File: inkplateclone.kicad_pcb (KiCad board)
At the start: 2 copper layers, 88 parts, among them J1 ED060SC7, J2 USB_C_Receptacle_USB2.0, J3 Conn_01x03_Male, Q1 Q_NMOS_GSD, Q2 Q_NMOS_GSD, Q3 Q_PMOS_GSD, U1 TPS65186, U2 ED097OC1, U3 MCP23017_SO, U4 ESP32-WROVER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

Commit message: routed switches and added 3d models
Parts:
- added J4: Conn_01x03_Male, Connector_PinHeader_2.54mm:PinHeader_1x03_P2.54mm_Vertical, F.Cu at (106.1, 125.4)
- added SW1: SW_Push, Button_Switch_SMD:SW_Push_1P1T_NO_6x6mm_H9.5mm, F.Cu at (125.6, 120.4)
- added SW2: SW_Push, Button_Switch_SMD:SW_Push_1P1T_NO_6x6mm_H9.5mm, F.Cu at (125.5, 112.0)
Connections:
- net /I2C_SCL renamed I2C_SCL
- net /I2C_SDA renamed I2C_SDA
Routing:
- net ESP_RXD: track 0.00 -> 15.5 mm
- net ESP_TXD: track 0.00 -> 12.5 mm
- net RST: track 4.19 -> 9.92 mm
- net EPD_CL: track 4.05 -> 9.63 mm
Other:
- board text added: "Flash"
- board text added: "GND"
- board text added: "RX"
- board text added: "Reset"
- board text added: "TX"

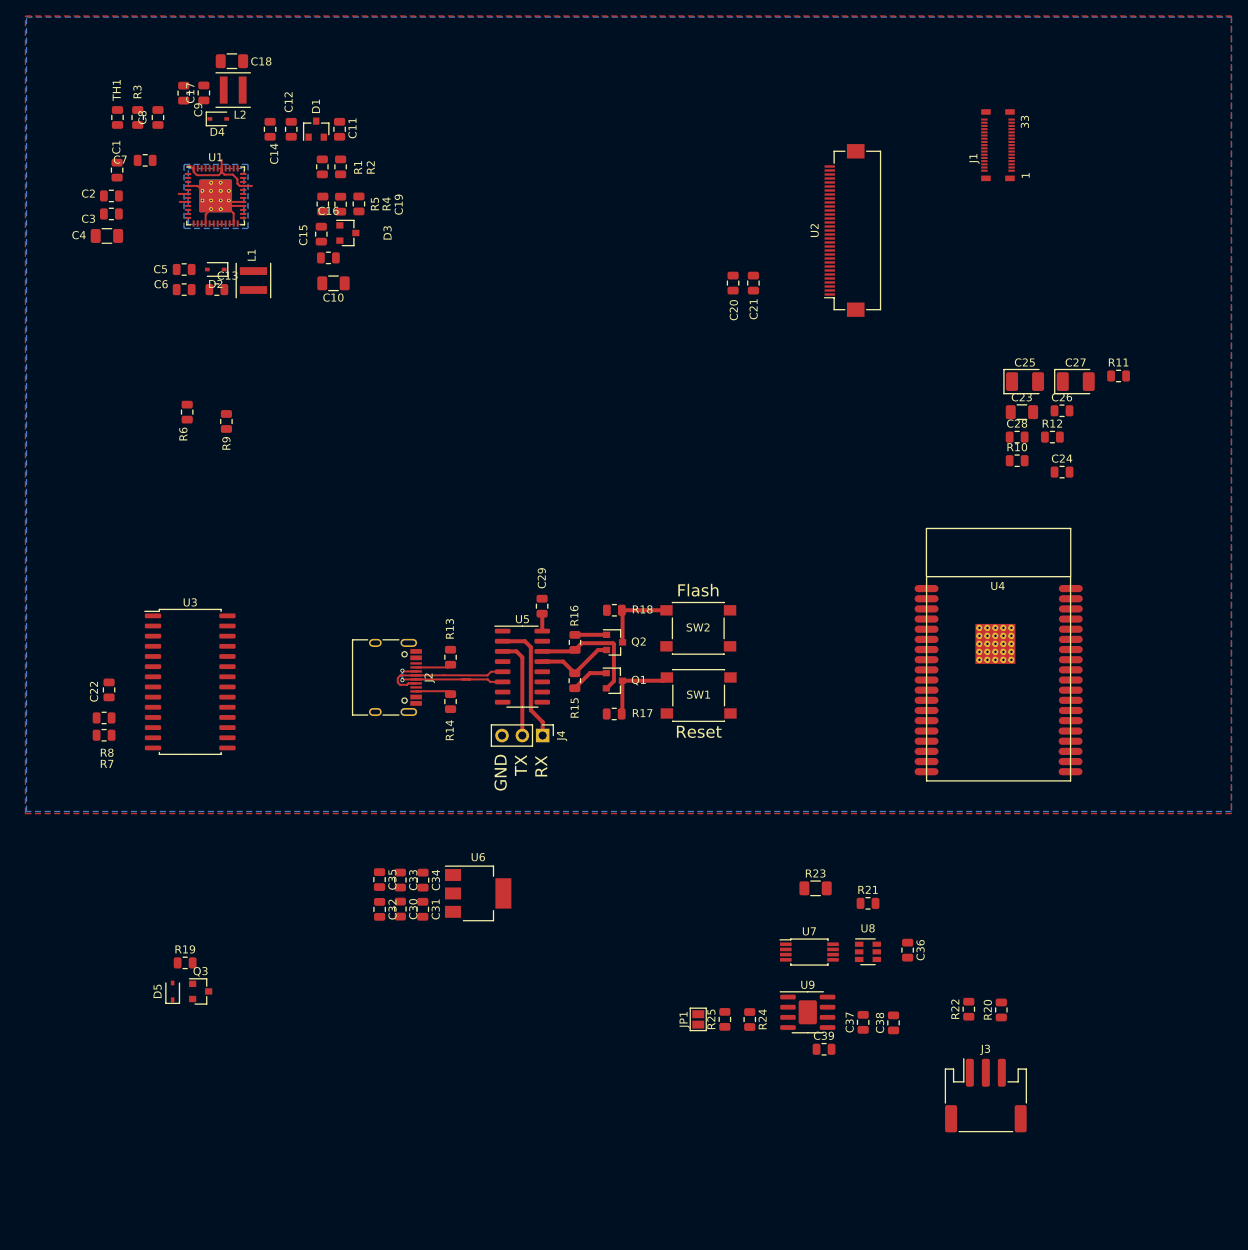
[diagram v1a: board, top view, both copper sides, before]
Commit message: routed charger and ideal diode
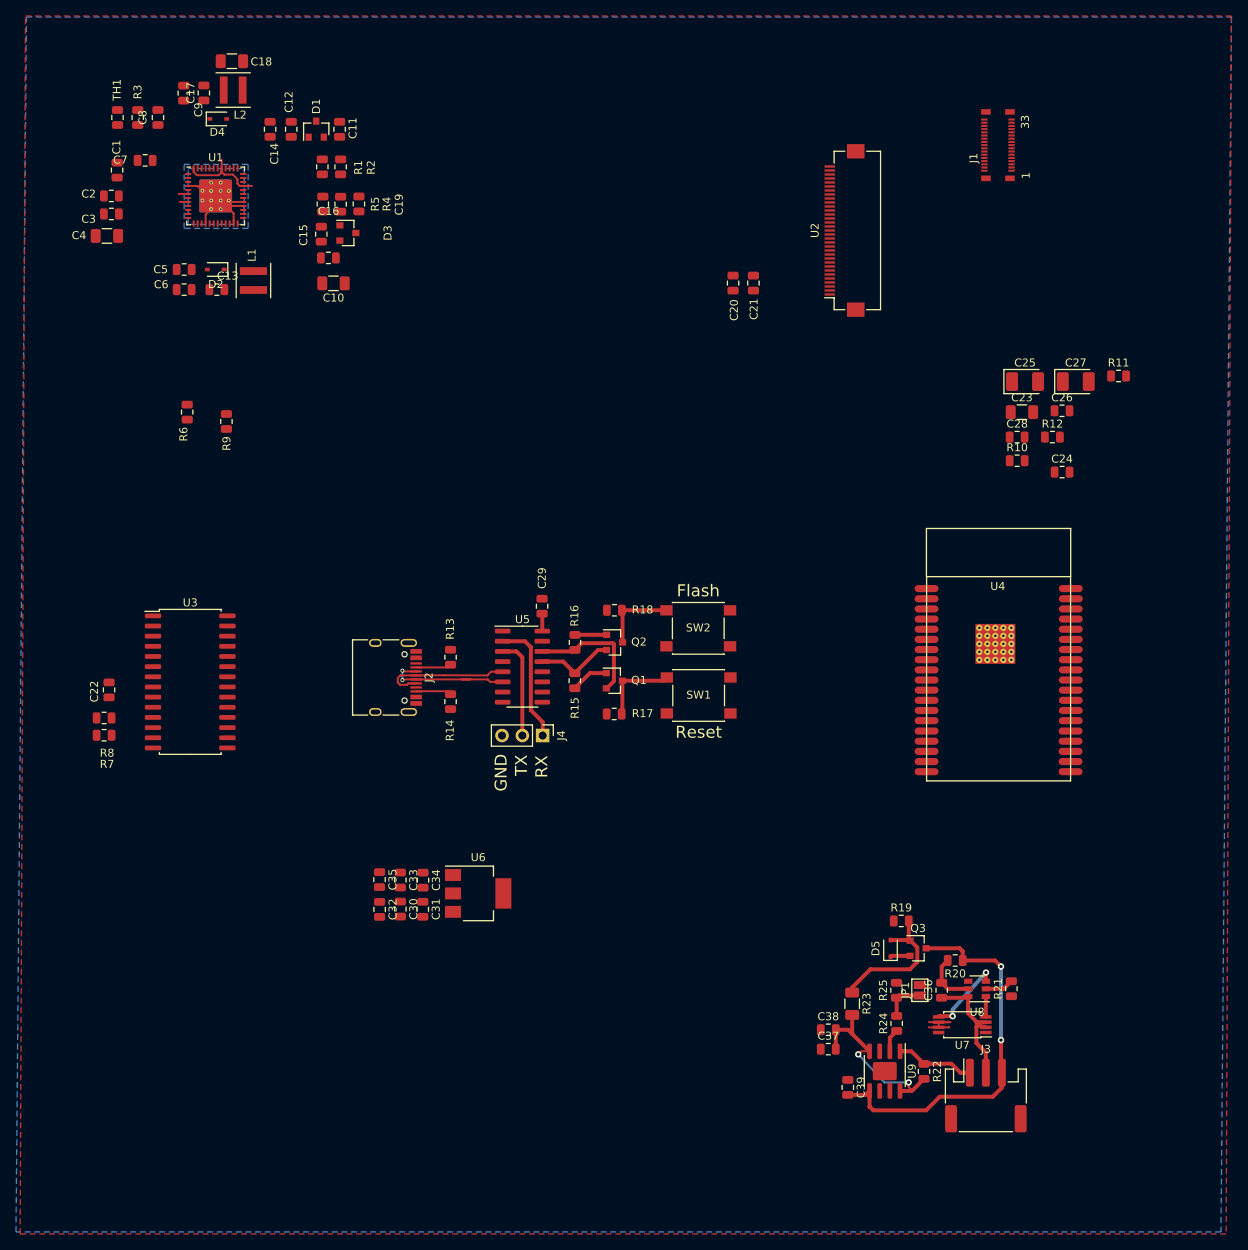
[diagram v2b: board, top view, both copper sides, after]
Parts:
- moved D5 89.9 mm to (149.5, 152.0)
- moved Q3 89.8 mm to (153.0, 152.0)
- moved R19 89.7 mm to (150.9, 148.6)
- moved JP1 27.9 mm to (153.2, 157.2)
- moved R25 21.8 mm to (150.3, 157.2)
- moved U7 21.2 mm to (158.5, 161.5), turned to 180 degrees
- moved R21 20.9 mm to (164.6, 157.0), turned to 90 degrees
- moved R24 18.4 mm to (150.3, 161.4), turned to 90 degrees
- moved R23 15.1 mm to (144.7, 158.9), turned to 270 degrees
- moved U8 14.4 mm to (160.4, 157.0), turned to 180 degrees
- moved U9 12.1 mm to (148.8, 167.3), turned to 270 degrees
- moved R22 9.58 mm to (153.7, 167.4), turned to 270 degrees
- moved R20 8.45 mm to (157.6, 153.5), turned to 180 degrees
- moved C38 8.20 mm to (141.8, 162.2), turned to 0 degrees
- moved C36 6.58 mm to (155.9, 157.2), turned to 90 degrees
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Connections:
- net /SPI_NCS renamed SPI_NCS
- net /SPI_SCL renamed SPI_SCL
- net /SPI_SDI renamed SPI_SDI
- J3 pad 3: /BAT_POS -> VBAT
- R20 pad 1: /BAT_POS -> VBAT
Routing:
- net VBAT: track 0.00 -> 49.0 mm, vias 0 -> 2
- net Net-(C37-Pad2): track 0.00 -> 24.4 mm, vias 0 -> 2
- net +5V: track 2.18 -> 20.3 mm
- net /BAT_GND: track 0.00 -> 16.4 mm
- net Net-(U7-Pad5): track 0.00 -> 9.92 mm, vias 0 -> 2
- net BAT_TMP: track 0.00 -> 9.86 mm
- net Net-(C36-Pad2): track 0.00 -> 6.74 mm
- net Net-(JP1-Pad1): track 0.00 -> 5.33 mm
- net GND: track 14.2 -> 19.4 mm
- net Net-(R21-Pad2): track 0.00 -> 3.58 mm
- net Net-(R24-Pad1): track 0.00 -> 2.89 mm
- net Net-(U7-Pad4): track 0.00 -> 2.54 mm
- net VIN: track 0.00 -> 2.50 mm

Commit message: routed voltage regulator
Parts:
- added J5: Conn_01x02_Male, Connector_PinHeader_2.54mm:PinHeader_1x02_P2.54mm_Vertical, F.Cu at (93.3, 125.4)
- moved C32 52.9 mm to (135.6, 164.7), turned to 0 degrees
- moved C35 50.9 mm to (131.9, 164.7), turned to 0 degrees
- moved C30 49.6 mm to (135.6, 162.1), turned to 0 degrees
- moved C33 47.5 mm to (131.9, 162.1), turned to 0 degrees
- moved C31 46.2 mm to (135.6, 159.3), turned to 0 degrees
- moved C34 43.8 mm to (132.0, 159.3), turned to 0 degrees
- moved U6 36.4 mm to (133.6, 152.4), turned to 90 degrees
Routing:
- net VIN: track 2.50 -> 27.5 mm
- net +3V3: track 0.00 -> 15.9 mm
- net RST: track 9.92 -> 17.9 mm
- net EPD_CL: track 9.63 -> 17.6 mm
- net +5V: track 20.3 -> 27.6 mm
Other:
- board text added: "+5v"

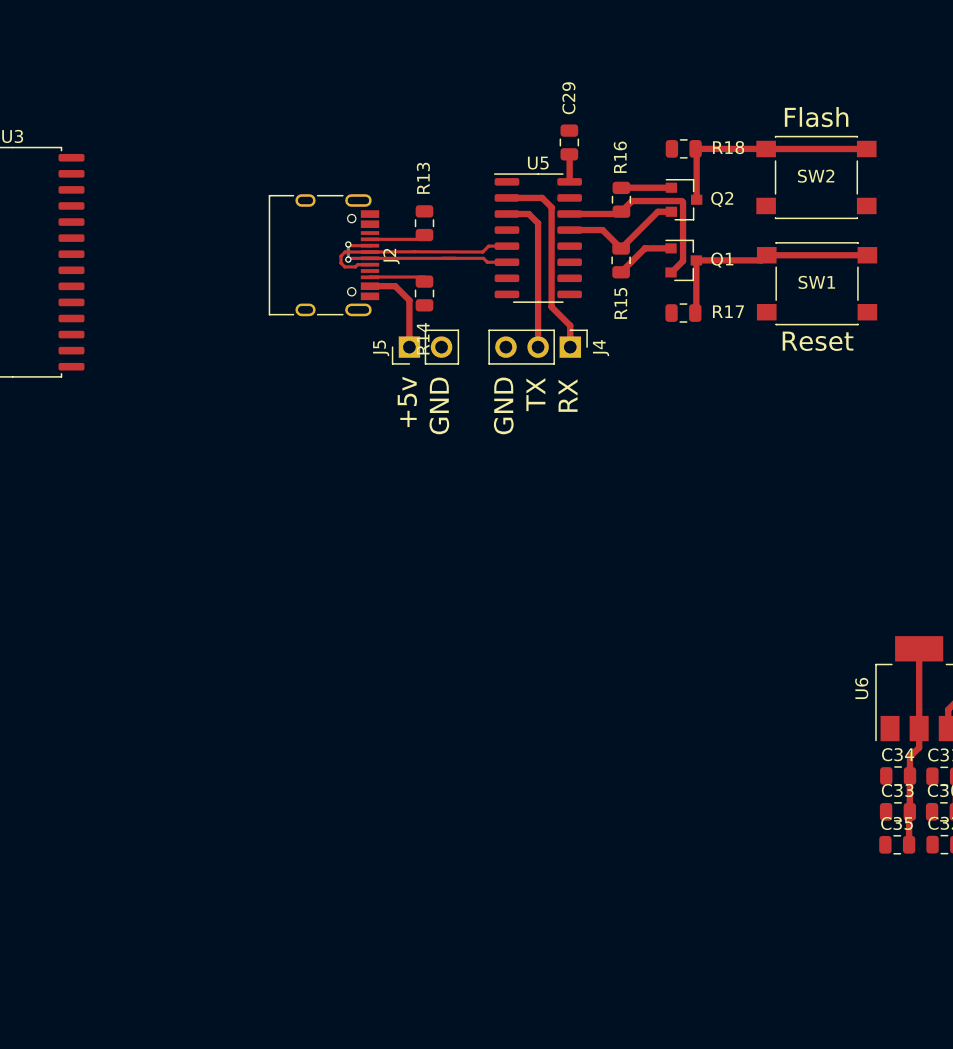
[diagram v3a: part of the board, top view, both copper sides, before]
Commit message: added 3d model for battery connector
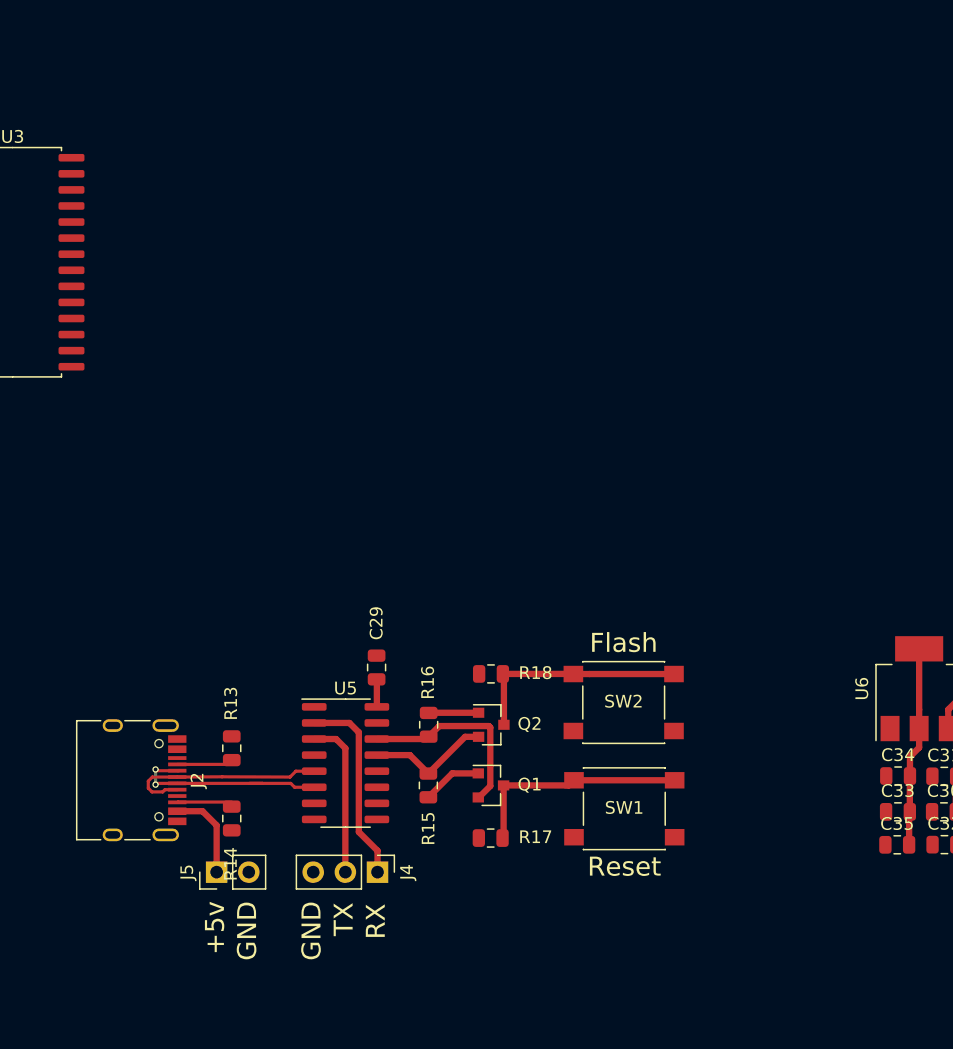
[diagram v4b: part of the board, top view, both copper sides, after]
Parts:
- moved J2 44.2 mm to (71.0, 159.6)
- moved Q1 44.2 mm to (99.8, 160.0)
- moved R15 44.2 mm to (94.8, 160.0)
- moved R18 44.2 mm to (99.8, 151.2)
- moved J4 44.2 mm to (90.8, 166.9)
- moved J5 44.2 mm to (78.1, 166.9)
- moved R13 44.2 mm to (79.3, 157.1)
- moved R17 44.2 mm to (99.8, 164.2)
- moved SW1 44.2 mm to (110.3, 161.8)
- moved SW2 44.2 mm to (110.3, 153.5)
- moved C29 44.2 mm to (90.8, 150.7)
- moved Q2 44.2 mm to (99.8, 155.2)
- moved R14 44.2 mm to (79.3, 162.6)
- moved R16 44.2 mm to (94.9, 155.2)
- moved U5 44.2 mm to (88.3, 158.2)

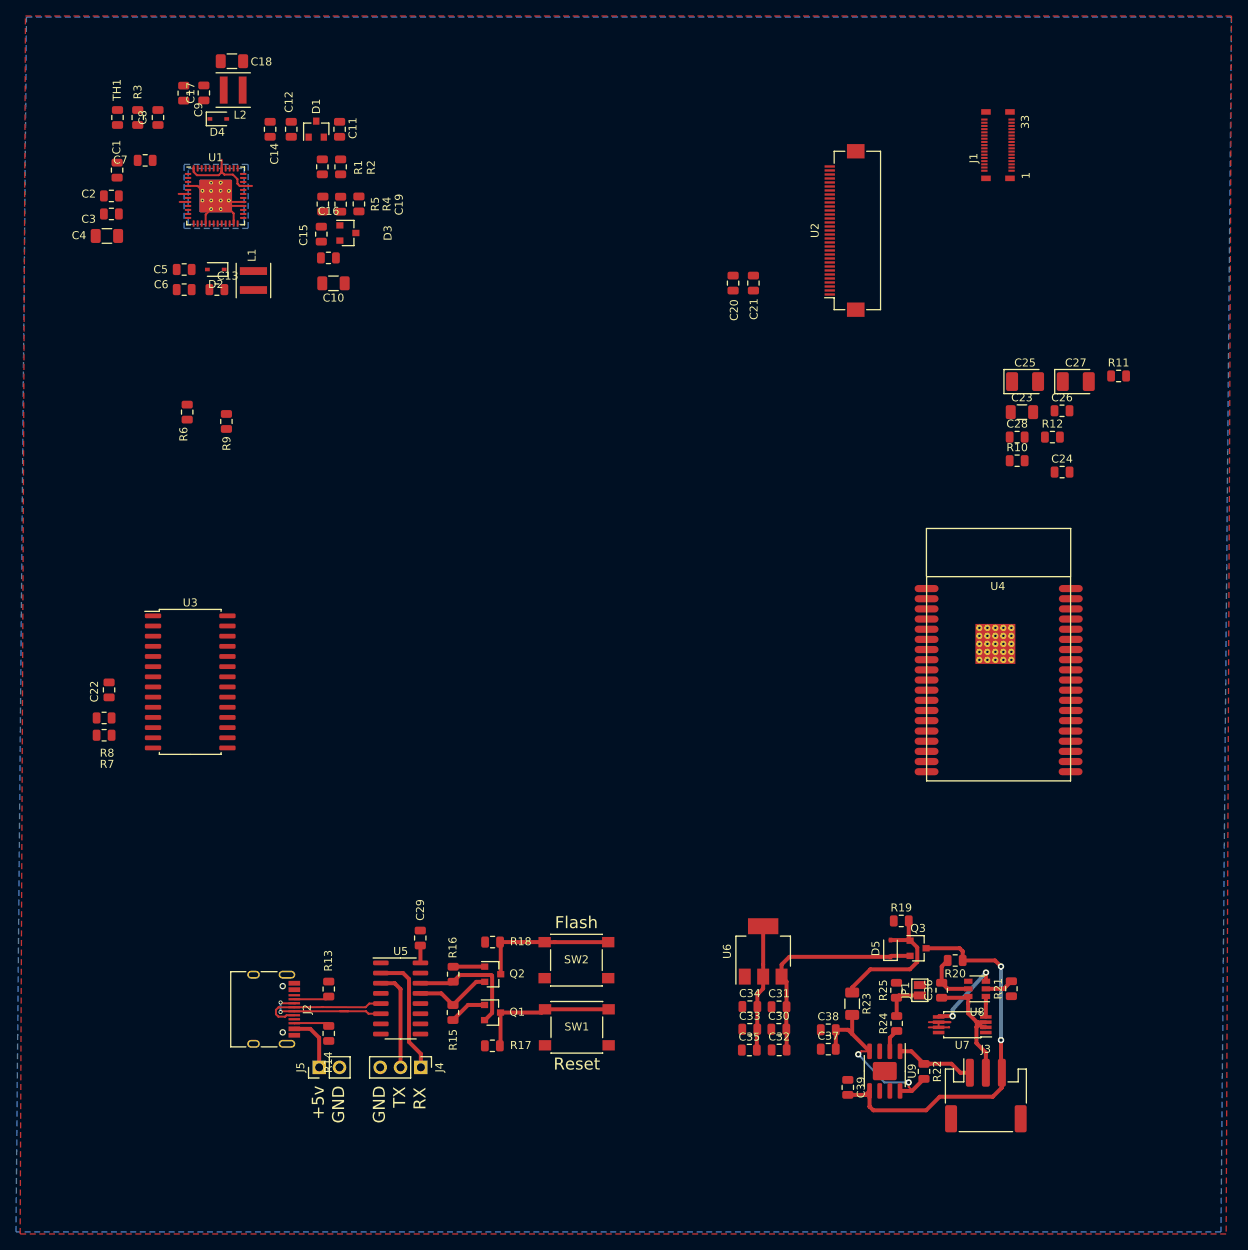
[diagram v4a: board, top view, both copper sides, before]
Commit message: cleaned up silkscreen
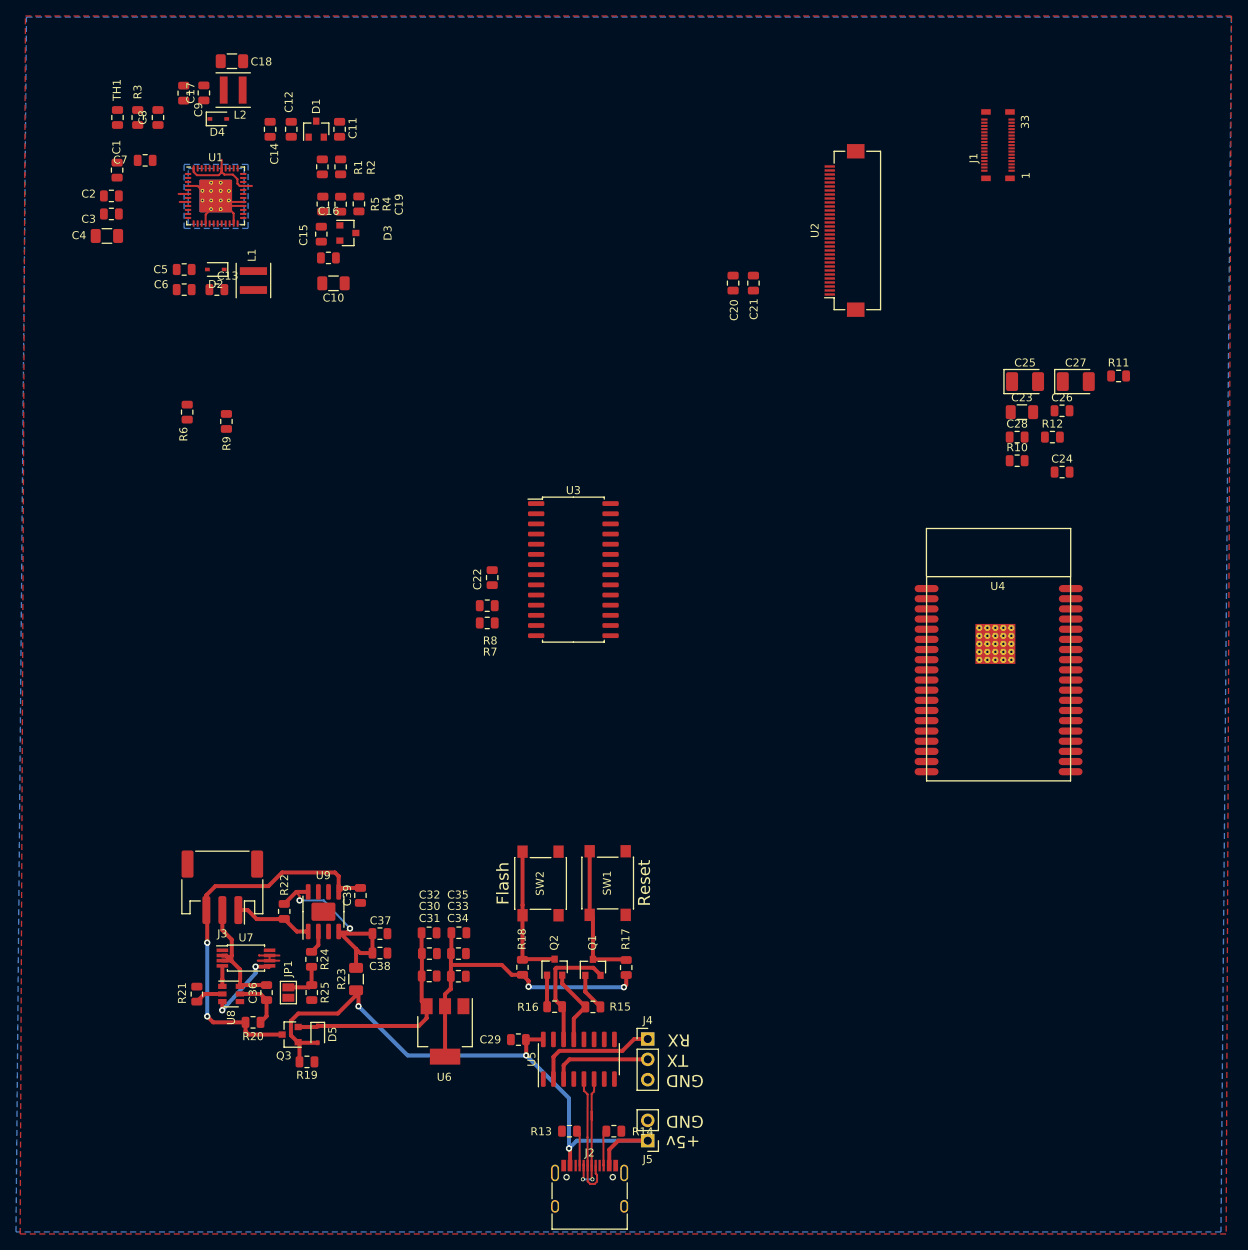
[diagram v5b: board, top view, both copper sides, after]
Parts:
- moved R21 101.8 mm to (62.8, 157.7), turned to 270 degrees
- moved J3 98.9 mm to (66.0, 144.3), turned to 180 degrees
- moved U8 93.2 mm to (67.1, 157.7), turned to 0 degrees
- moved U7 89.9 mm to (69.0, 153.2), turned to 0 degrees
- moved R20 88.1 mm to (69.8, 161.2), turned to 0 degrees
- moved C36 84.4 mm to (71.5, 157.5), turned to 270 degrees
- moved R22 82.4 mm to (73.7, 147.4), turned to 90 degrees
- moved Q3 79.2 mm to (74.5, 162.8), turned to 180 degrees
- moved JP1 78.9 mm to (74.3, 157.5), turned to 270 degrees
- moved R19 76.3 mm to (76.6, 166.2), turned to 180 degrees
- moved R24 73.6 mm to (77.2, 153.4), turned to 270 degrees
- moved R25 73.1 mm to (77.2, 157.5), turned to 270 degrees
- moved U9 72.9 mm to (78.7, 147.4), turned to 90 degrees
- moved D5 72.4 mm to (77.9, 162.7), turned to 270 degrees
- moved C39 65.5 mm to (83.3, 145.4), turned to 90 degrees
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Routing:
- net +5V: track 27.6 -> 81.5 mm, vias 0 -> 3
- net +3V3: track 15.9 -> 40.7 mm, vias 0 -> 2
- net Net-(C37-Pad2): track 24.4 -> 28.7 mm
